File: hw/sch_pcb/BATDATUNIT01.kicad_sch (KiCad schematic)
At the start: 119 parts, among them IC1 MAX14502AETL+, J1 USBC_USB4105-GF-A, J22 HEADER_2x03, J4 46436-9327, J9 SD_Card-FPS009-4200-0, Q1 BC817-25, Q2 BC817-25, Q3 BC817-25, Q4 BC817-25, SW1 SKRTLAE010, SW2 KMT031, SW3 SKRTLAE010, SW4 KMT031, U10 ATMEGA1284P-AU, U11 PCF85263A, U11 TCA4307, U2 USBLC6-2SC6, U3 FT260Q-T, U4 PCA9541ABS/01, U6 AT24CS64-SSHM, U6 SHT31-DIS, U7 TMUX1574DYYR, Y1 19.2 MHz, Y1 8 MHz, Y2 ABS07-120-32.768KHZ-T

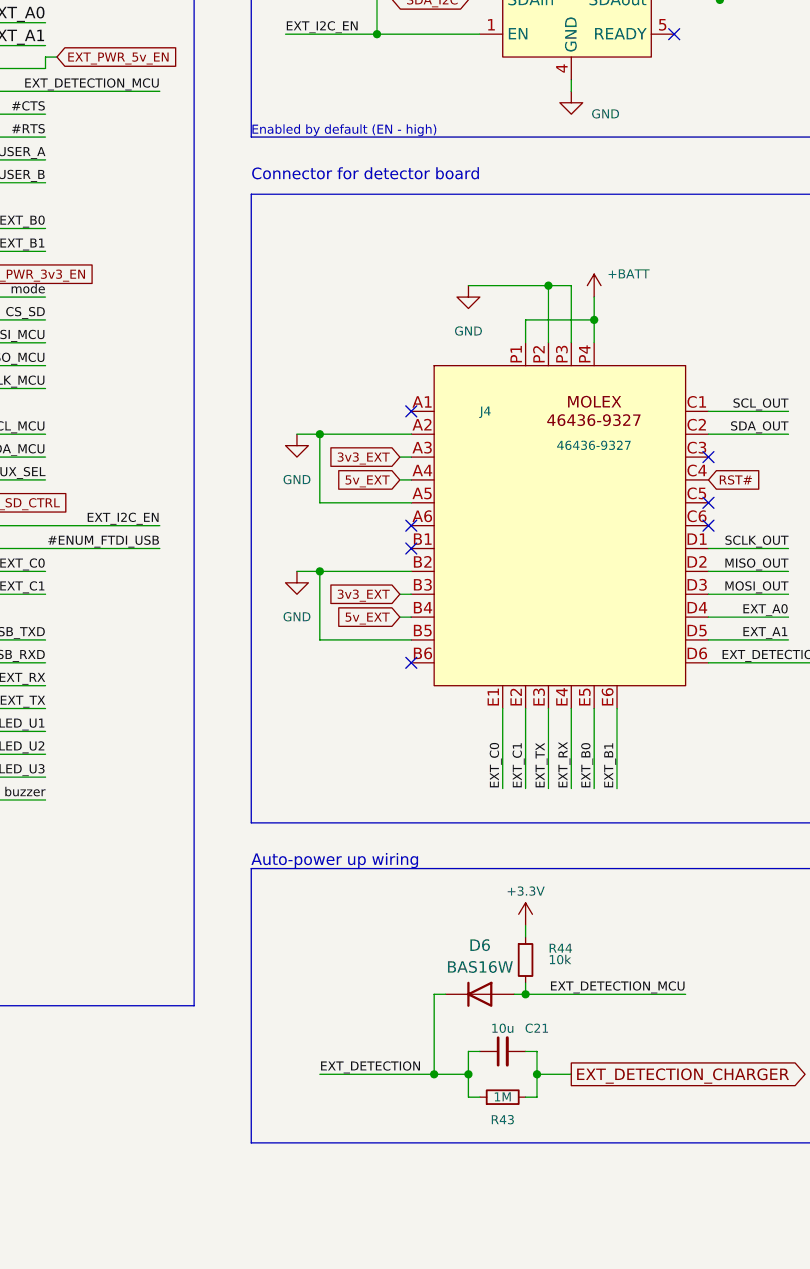
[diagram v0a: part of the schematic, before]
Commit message: Improve automatic power up reliability by changing power up circuit components values.
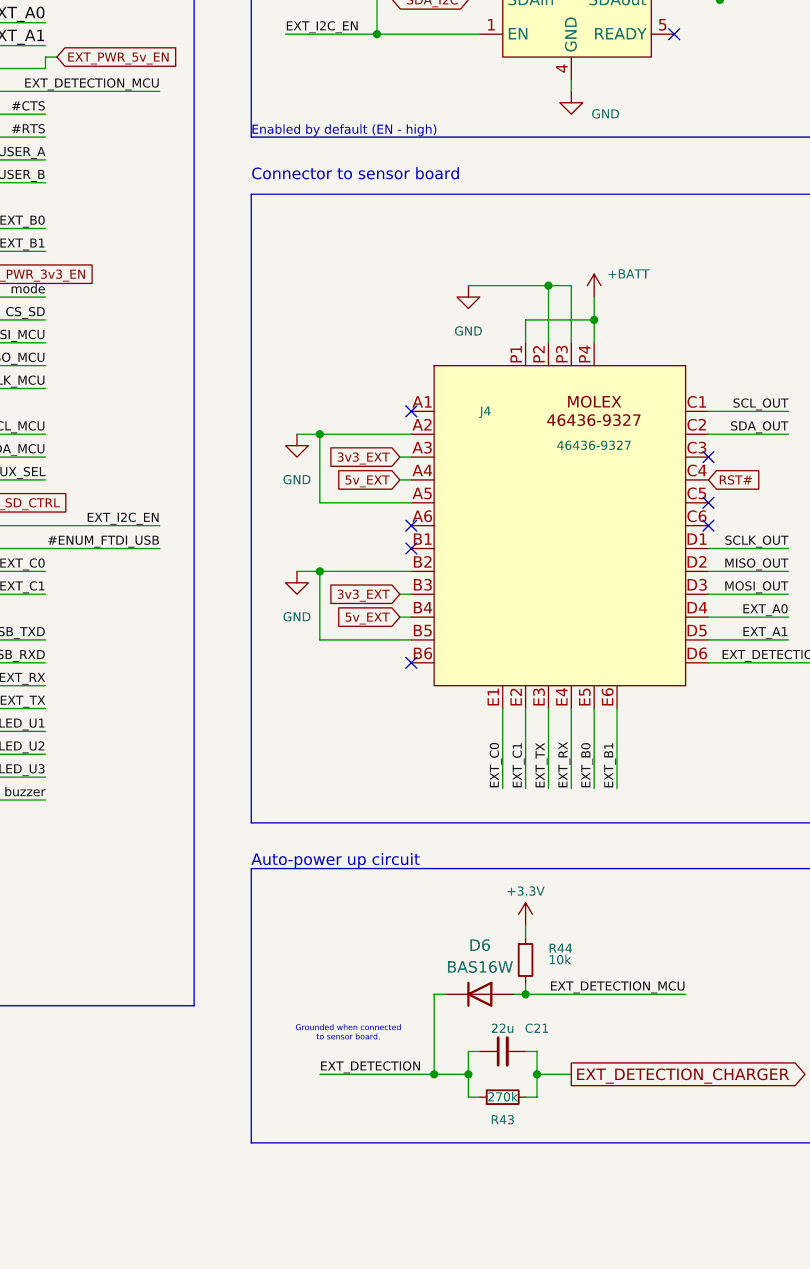
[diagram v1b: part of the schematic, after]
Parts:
- C21: value 10u -> 22u; UST_ID 5c70984712875079b91f8b53 -> 650b58f1462c6d9e7205463b
- R43: value 1M -> 270k; UST_ID 5c70984712875079b91f8aaa -> 5c70984712875079b91f8aa0
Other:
- note added: "Auto-power up circuit"
- note added: "Connector to sensor board"
- note added: "Grounded when connected to sensor board."
- note removed: "Auto-power up wiring"
- note removed: "Connector for detector board"

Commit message: Convert to KiCAD 9 Add CR2032 battery holder to avoid RTC reset with removed accumulators.
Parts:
- removed JP4: SolderJumper_2_Open, Jumper:SolderJumper-2_P1.3mm_Bridged_RoundedPad1.0x1.5mm, symbol Jumper:SolderJumper_2_Bridged
- added BT3: CR2032, Battery:BatteryHolder_Keystone_1060_1x2032, symbol Device:Battery_Cell
- added C51, C52: 100n, Capacitor_SMD:C_0805_2012Metric, symbol Device:C_Small
- R41: renamed from R17; now not fitted
- gave numbers to parts that had none: 7
- renumbered C6 to C1, C26 to C10, C40 to C11, C43 to C12, C27 to C13, C33 to C14, C44 to C15, C36 to C17, C47 to C19, C5 to C2, C60 to C20, C7 to C3, C7 to C4, C36 to C50, C30 to C9, J9 to J2, J22 to J3, JP1 to JP3, R17 to R10, R17 to R11, R23 to R12, R20 to R21, R21 to R23, R20 to R24, R21 to R25, R20 to R36, R21 to R37, R32 to R38, R23 to R40, R21 to R42, R23 to R45, R20 to R46, R21 to R47, R17 to R6, R17 to R7, R17 to R8, R17 to R82, R17 to R9, IC1 to U1, U11 to U10, U6 to U5, U10 to U8, Y1 to Y2, Y2 to Y3
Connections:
- net +3.3V: now also C51.1, C52.1
- net GND: now also BT3.2 (-), C51.2, C52.2
- net at R41.1: now also C20.1, U10.3 (VBAT), BT3.1 (+)
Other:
- title: BATDATUNTI01 -> BATDATUNIT01C

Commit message: Update UST_IDs.
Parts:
- R13: UST_ID (none) -> 5c70984712875079b91f8a91
- R4: UST_ID (none) -> 5fa0fc3e12875025b3977997
- R46, R47: UST_ID 5c70984512875079b91f898c -> 5c70984612875079b91f899f
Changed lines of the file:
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@@
 			)
 		)
-		(property "UST_ID" "5c70984512875079b91f898c"
+		(property "UST_ID" " 5c70984612875079b91f899f"
 			(at 389.89 116.84 0)
 			(effects
@@
 			)
 		)
-		(property "UST_ID" "5c70984512875079b91f898c"
+		(property "UST_ID" " 5c70984612875079b91f899f"
 			(at 387.35 116.84 0)
 			(effects
@@
 			)
 		)
+		(property "UST_ID" "5fa0fc3e12875025b3977997"
+			(at 101.6 199.39 0)
+			(effects
+				(font
+					(size 1.27 1.27)
+				)
+				(hide yes)
+			)
+		)
 		(pin "1"
 		)
@@
 			)
 		)
-		(property "UST_ID" ""
+		(property "UST_ID" "5c70984712875079b91f8a91"
 			(at 109.22 121.92 0)
 			(effects

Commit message: Repair white characters in UST_ID fields.
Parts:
- R46, R47: UST_ID 5c70984612875079b91f899f -> 5c70984612875079b91f899f
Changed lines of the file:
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@@
 			)
 		)
-		(property "UST_ID" " 5c70984612875079b91f899f"
+		(property "UST_ID" "5c70984612875079b91f899f"
 			(at 389.89 116.84 0)
 			(effects
@@
 			)
 		)
-		(property "UST_ID" " 5c70984612875079b91f899f"
+		(property "UST_ID" "5c70984612875079b91f899f"
 			(at 387.35 116.84 0)
 			(effects

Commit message: Fix attributes of some components.
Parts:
- BT3: UST_ID (none) -> 68249eacee7fc534862c6977
- TP1, TP2: now left out of the parts list
- Y1: UST_ID (none) -> 67f16090ee7fc534862c5860
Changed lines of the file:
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@@
 		(unit 1)
 		(exclude_from_sim no)
-		(in_bom yes)
+		(in_bom no)
 		(on_board yes)
 		(dnp no)
@@
 			)
 		)
+		(property "UST_ID" "68249eacee7fc534862c6977"
+			(at 336.55 83.82 0)
+			(effects
+				(font
+					(size 1.27 1.27)
+				)
+				(hide yes)
+			)
+		)
 		(pin "1"
 		)
@@
 		(unit 1)
 		(exclude_from_sim no)
-		(in_bom yes)
+		(in_bom no)
 		(on_board yes)
 		(dnp no)
@@
 			(at 92.71 189.23 0)
 			(effects
+				(font
+					(size 1.27 1.27)
+				)
+				(hide yes)
+			)
+		)
+		(property "UST_ID" "67f16090ee7fc534862c5860"
+			(at 92.71 189.23 0)
+			(effects

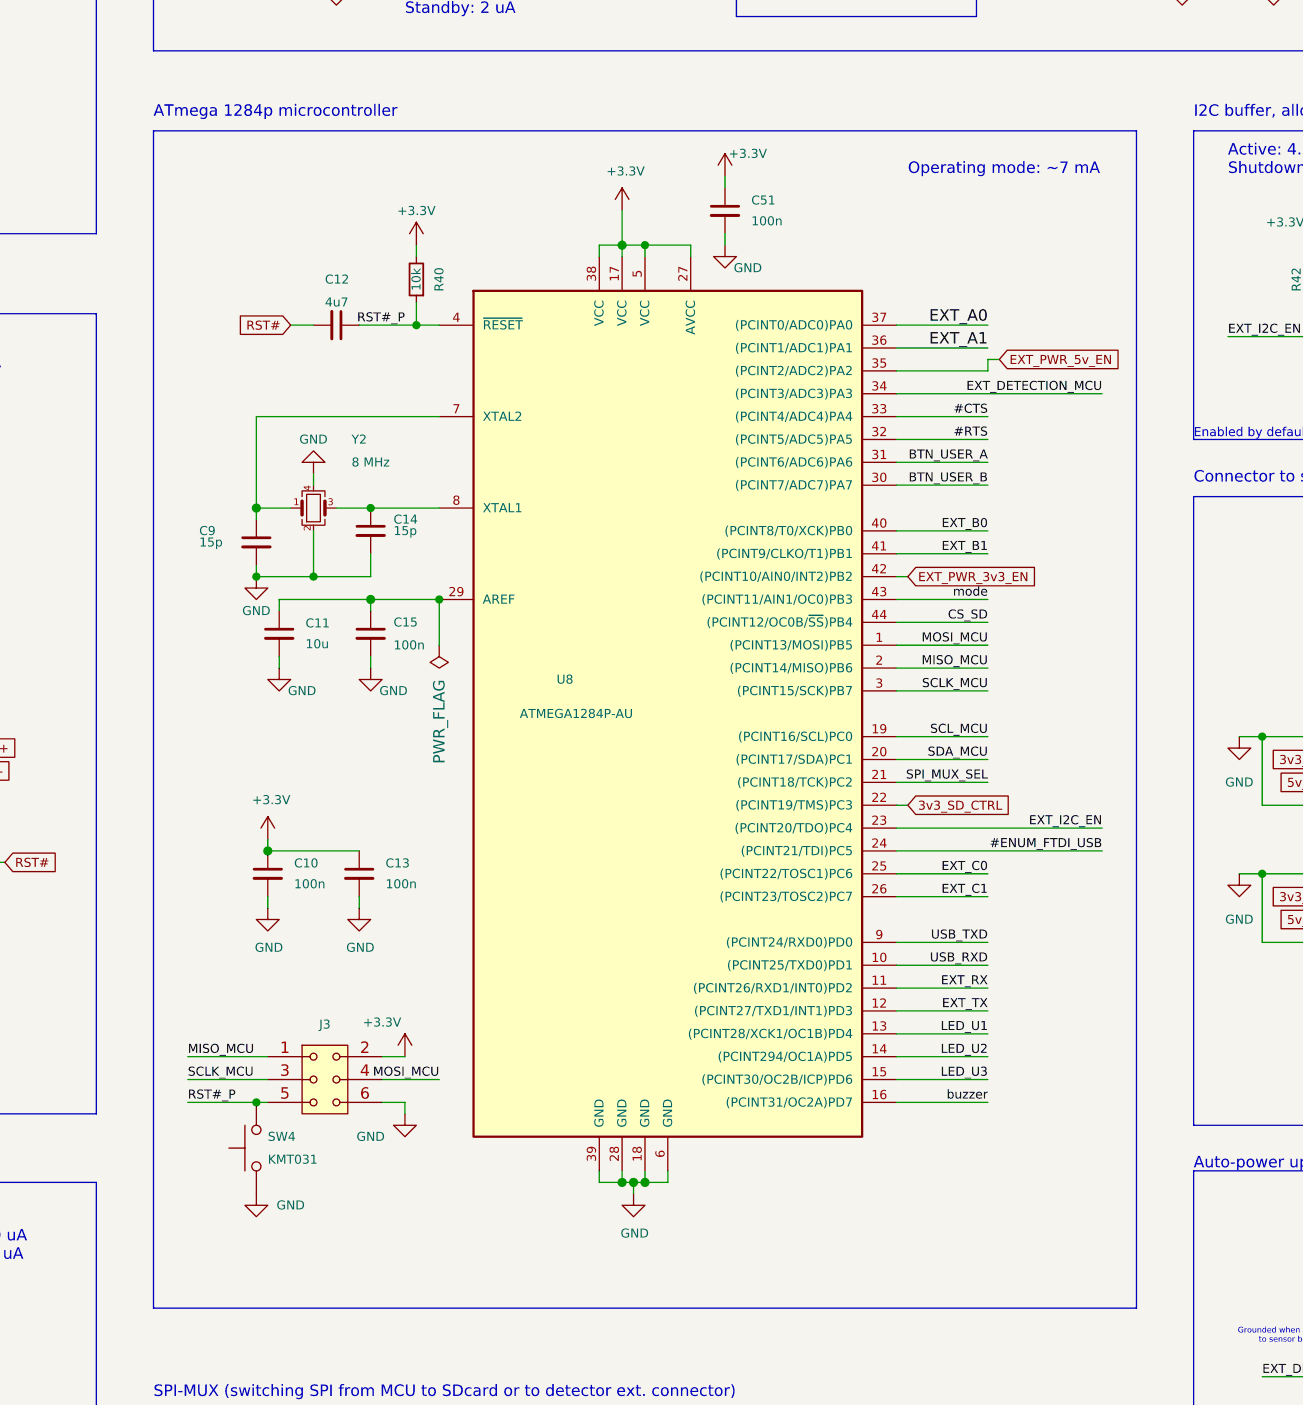
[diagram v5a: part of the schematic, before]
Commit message: Update ATmega symbol.
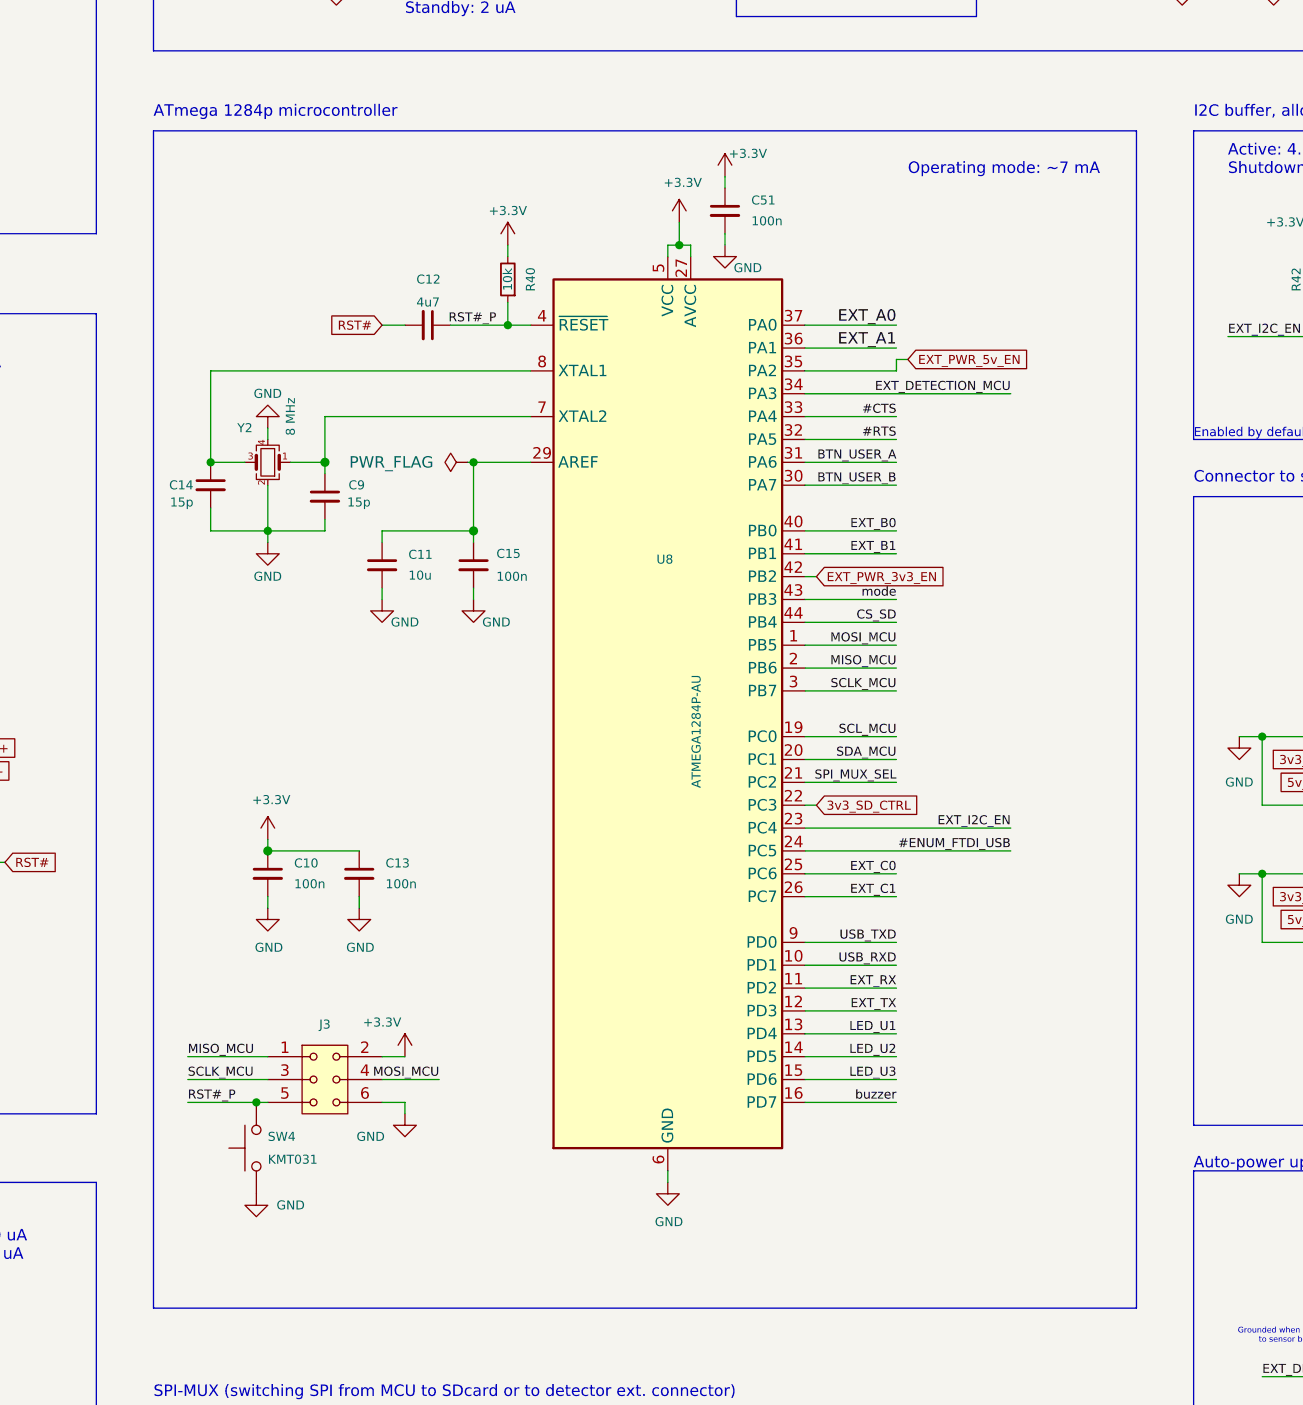
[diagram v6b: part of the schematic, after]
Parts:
- U8: symbol SPACEDOS01A_PCB01A-rescue:ATMEGA1284P-AU-atmel-DATALOGGER01A-rescue-CCP2019V01A-rescue -> MCU_Microchip_ATmega:ATmega1284P-A
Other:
- moved on the sheet: C11, C12, C14, C15, C9, R40, Y2
